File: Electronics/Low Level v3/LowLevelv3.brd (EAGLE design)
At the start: 117.3 x 68.1 mm, 53 parts, among them IC2 MCP4802, K1 ORWH-SH-105D1F,000, K3 ORWH-SH-105D1F,000, Q1 16MHz, T1 2N3904, T2 2N3904, U1 284512-4, U4 MCP2515, U5 MCP2551DIL08, X3 Motor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

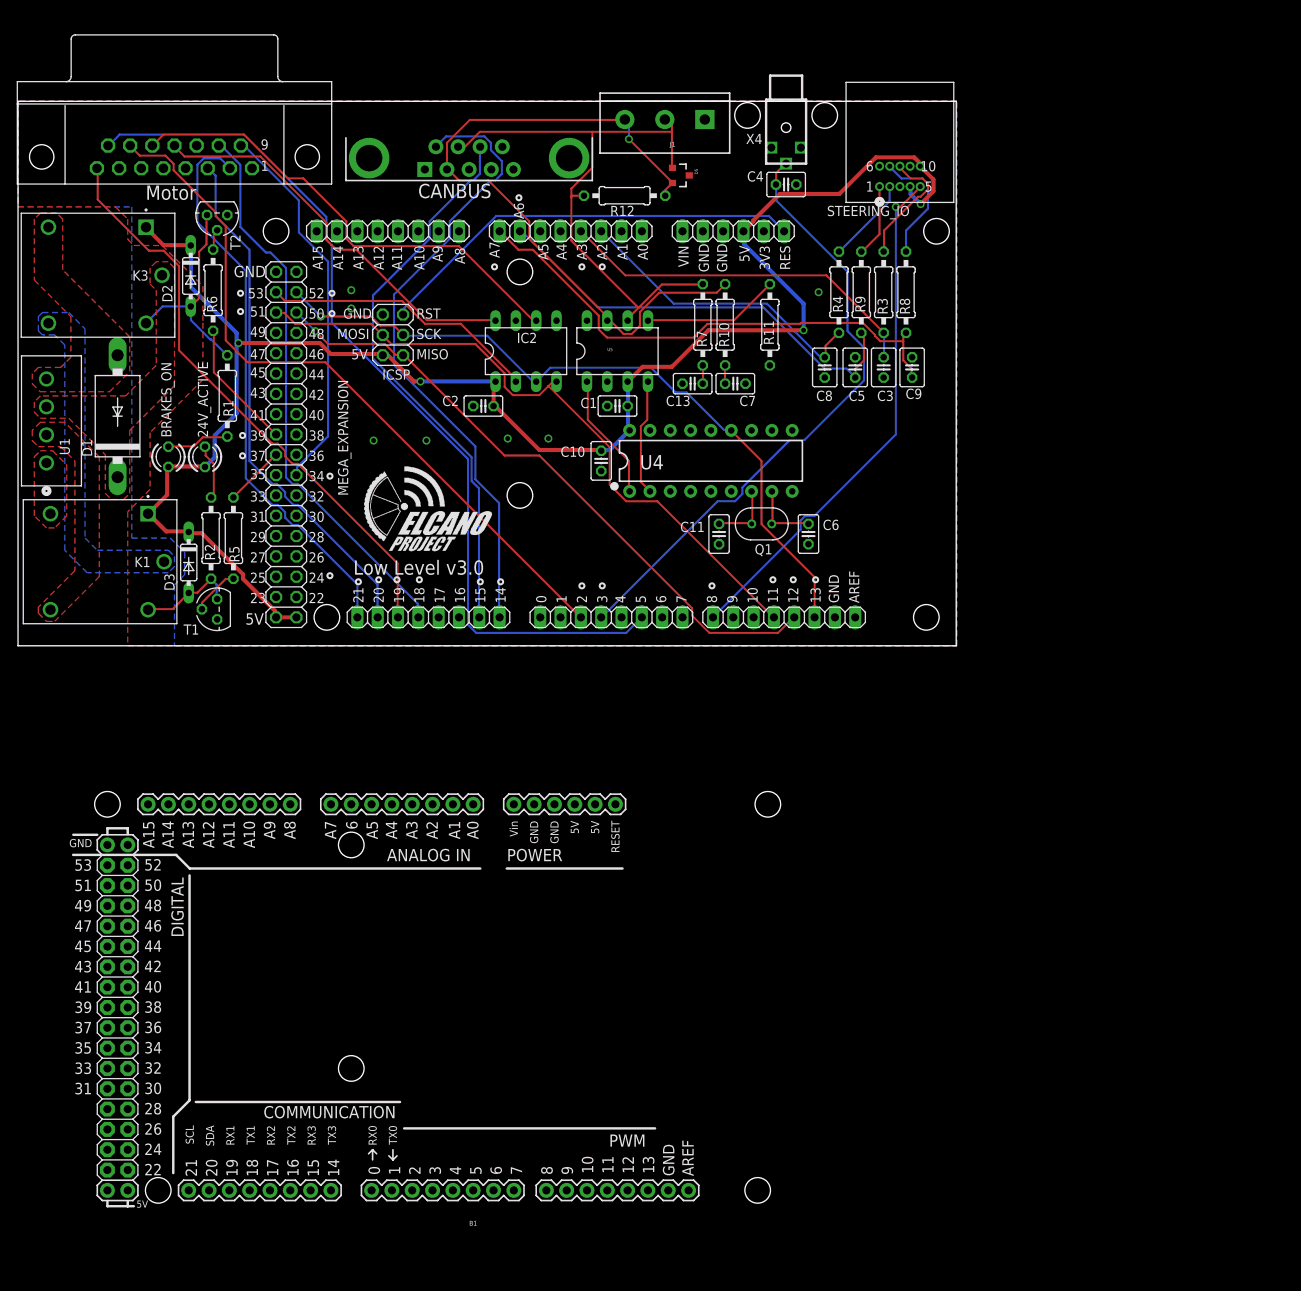
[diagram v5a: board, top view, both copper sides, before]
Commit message: Added reset button to top of board
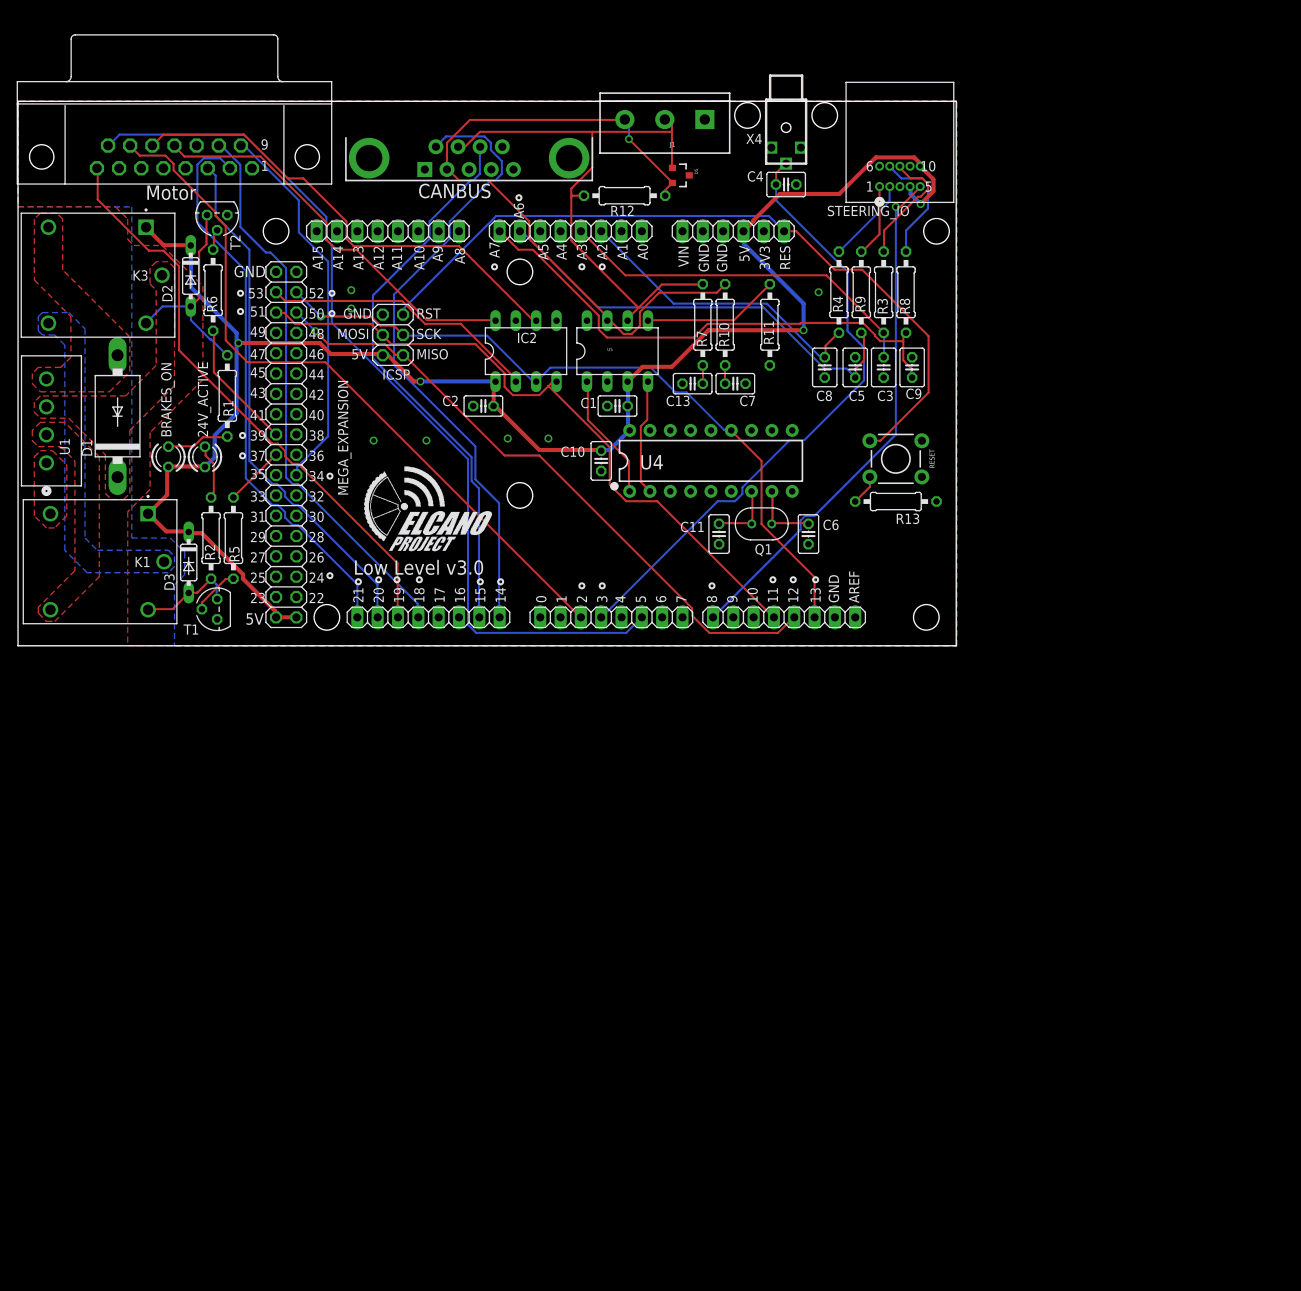
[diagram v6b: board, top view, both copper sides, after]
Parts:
- removed B1: ARDUINO_MEGA_R3FULL, SparkFun-Boards:ARDUINO_MEGA
- added R13: 1K, rcl:0207/10
- added RESET: MOMENTARY-SWITCH-SPST-PTH-6.0MM, SparkFun-Switches:TACTILE_SWITCH_PTH_6.0MM
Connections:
- new net N$1: R13.2, RESET.3
- net GND: now also R13.1
- net RESET: now also RESET.1
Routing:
- net RESET: track 53.9 -> 94.3 mm
- net N$1: track 0.00 -> 3.83 mm
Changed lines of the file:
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@@
 <attribute name="VALUE" x="77.3176" y="62.484" size="1.27" layer="27" ratio="10" rot="R180"/>
 </element>
-<element name="B1" library="SparkFun-Boards" library_urn="urn:adsk.eagle:library:509" package="ARDUINO_MEGA" package3d_urn="urn:adsk.eagle:package:37320/1" value="ARDUINO_MEGA_R3FULL" x="59.182" y="-38.354" smashed="yes" rot="R180">
-<attribute name="NAME" x="57.912" y="-66.294" size="0.6096" layer="25" font="vector" ratio="20" rot="R180" align="bottom-center"/>
-<attribute name="VALUE" x="59.182" y="-10.414" size="0.6096" layer="27" font="vector" ratio="20" rot="R180" align="top-center"/>
+<element name="RESET" library="SparkFun-Switches" library_urn="urn:adsk.eagle:library:535" package="TACTILE_SWITCH_PTH_6.0MM" package3d_urn="urn:adsk.eagle:package:40163/1" value="MOMENTARY-SWITCH-SPST-PTH-6.0MM" x="110.744" y="28.956" smashed="yes">
+<attribute name="NAME" x="115.57" y="28.956" size="0.6096" layer="25" font="vector" ratio="20" rot="R90" align="bottom-center"/>
+<attribute name="PROD_ID" value=" SWCH-08441" x="110.744" y="28.956" size="1.778" layer="27" display="off"/>
+<attribute name="SF_SKU" value="COM-00097" x="110.744" y="28.956" size="1.778" layer="27" display="off"/>
+</element>
+<element name="R13" library="rcl" library_urn="urn:adsk.eagle:library:334" package="0207/10" package3d_urn="urn:adsk.eagle:package:23491/2" value="1K" x="110.744" y="23.622" smashed="yes" rot="R180">
+<attribute name="NAME" x="113.792" y="22.098" size="1.27" layer="25" ratio="10" rot="R180"/>
+<attribute name="SPICEPREFIX" value="R" x="110.744" y="23.622" size="1.778" layer="27" rot="R180" display="off"/>
+<attribute name="VALUE" x="113.0046" y="24.257" size="1.27" layer="27" ratio="10" rot="R180"/>
 </element>
 </elements>
@@
 <via x="67.31" y="31.496" extent="1-16" drill="0.6096"/>
 <via x="101.092" y="49.784" extent="1-16" drill="0.6096"/>
+<contactref element="R13" pad="1"/>
 </signal>
 <signal name="RESET">
@@
 <wire x1="96.6978" y1="57.4929" x2="94.869" y2="59.3217" width="0.254" layer="16"/>
 <wire x1="96.6978" y1="57.4929" x2="96.774" y2="57.404" width="0.254" layer="16"/>
+<contactref element="RESET" pad="1"/>
+<wire x1="103.0986" y1="52.6034" x2="98.298" y2="57.404" width="0.254" layer="1"/>
+<wire x1="98.298" y1="57.404" x2="96.774" y2="57.404" width="0.254" layer="1"/>
+<wire x1="114.8334" y1="37.232475" x2="108.817525" y2="31.2166" width="0.254" layer="1"/>
+<wire x1="107.4928" y1="31.2166" x2="108.817525" y2="31.2166" width="0.254" layer="1"/>
+<wire x1="114.8334" y1="37.232475" x2="114.8334" y2="44.301525" width="0.254" layer="1"/>
+<wire x1="114.8334" y1="44.301525" x2="106.531525" y2="52.6034" width="0.254" layer="1"/>
+<wire x1="106.531525" y1="52.6034" x2="103.0986" y2="52.6034" width="0.254" layer="1"/>
 </signal>
 <signal name="SPEEDOMETER">
@@
 <wire x1="111.32904375" y1="60.452" x2="113.4745" y2="62.59745625" width="0.254" layer="1"/>
 </signal>
+<signal name="N$1">
+<contactref element="R13" pad="2"/>
+<contactref element="RESET" pad="3"/>
+<wire x1="105.664" y1="23.622" x2="107.4928" y2="25.4508" width="0.254" layer="1"/>
+<wire x1="107.4928" y1="25.4508" x2="107.4928" y2="26.6954" width="0.254" layer="1"/>
+</signal>
 </signals>

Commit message: Many LLBv3 updates in one!
re-arranged inerrupt pins to share a PCI ISR, added RC circuit to MCP2515 per datasheet, replaced impossible capacitor, re-arranged oscilator layout
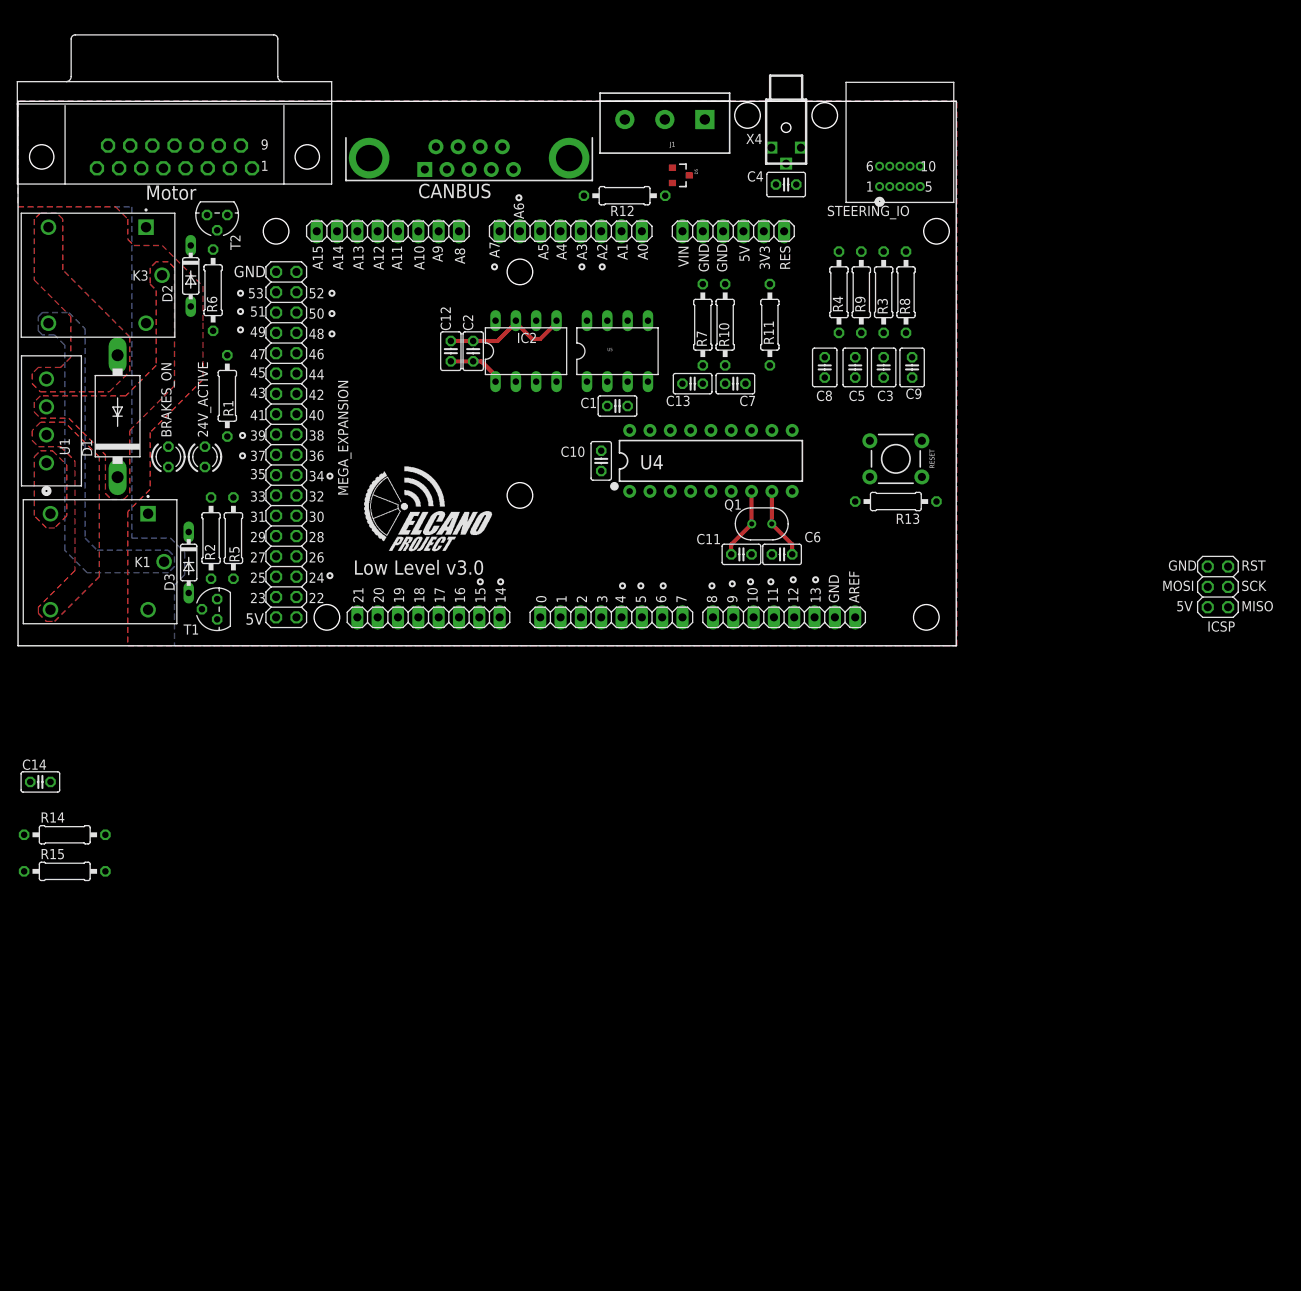
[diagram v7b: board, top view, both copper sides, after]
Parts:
- added C12, C14: 0.1uF, rcl:C025-025X050
- added R14: 1K, rcl:0207/10
- added R15: 20K, rcl:0207/10
- C11, C6: value 22pF -> 33pF
- C2: value 0.2uF -> 0.1uF
- moved ICSP 107.8 mm to (151.0, 13.0)
- moved C2 6.97 mm to (57.9, 42.4), turned to 90 degrees
- moved C6 4.17 mm to (96.5, 17.0), turned to 180 degrees
- moved C11 3.78 mm to (91.4, 17.0), turned to 0 degrees
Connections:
- net SL_RET renamed L_RET
- net SL_RTN renamed L_RTN_GND
- net SR_RET renamed R_RET
- net SR_RTN renamed R_RTN_GND
- removed net 3MISO: DIGITAL_8-13.5, ICSP.1, MEGA_EXPANSION.6
- removed net 3MOSI: DIGITAL_8-13.4, IC2.4, ICSP.4, MEGA_EXPANSION.5
- removed net CAN_CS: U4.16
- removed net SELECTAB: IC2.2, MEGA_EXPANSION.3
- new net CAN_SS: MEGA_EXPANSION.7, U4.16
- new net DAC_SS: IC2.2, MEGA_EXPANSION.8
- new net L_SENSE: C8.1, R4.1
- new net N$4: C14.1, R14.2, R15.2
- new net R_SENSE: C3.1, R3.1
- new net SPI_SLAVE: MEGA_EXPANSION.3
- net 5V: now also C12.1, R15.1
- net CAN_INT: now also DIGITAL_0-7.5
- net EBIKECONTRL: now also DIGITAL_8-13.3; no longer DIGITAL_14-21.4
- net GND: now also C12.2, C14.2, DIGITAL_8-13.7
- net HALLPHASEA: now also DIGITAL_8-13.6; no longer DIGITAL_14-21.1
- net HALLPHASEB: now also DIGITAL_8-13.5; no longer DIGITAL_14-21.2
- net HALLPHASEC: now also DIGITAL_8-13.4; no longer DIGITAL_14-21.3
- net MISO: now also ICSP.1, MEGA_EXPANSION.6
- net MOSI: now also IC2.4, ICSP.4, MEGA_EXPANSION.5
- net RS: now also R14.1
- net SCK: no longer DIGITAL_8-13.6
- net SPEEDOMETER: now also DIGITAL_8-13.1; no longer DIGITAL_0-7.3
- net STEER_SERVO_PWM: now also DIGITAL_0-7.7; no longer DIGITAL_8-13.1
- net STR_L: no longer C8.1, R4.1
- net STR_R: no longer C3.1, R3.1
- net WHEELROTATION: now also DIGITAL_8-13.2; no longer DIGITAL_0-7.4
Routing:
- net 5V: track 214.4 -> 7.09 mm, vias 4 -> 0
- net WATCHDOG: track 113.4 -> 0.00 mm
- net RESET: track 94.3 -> 0.00 mm
- net SCK: track 90.7 -> 0.00 mm, vias 1 -> 0
- net SPEEDOMETER: track 89.9 -> 0.00 mm
- net CANL: track 87.6 -> 0.00 mm, vias 1 -> 0
- net 3MOSI: track 84.0 -> 0.00 mm
- net 3MISO: track 80.2 -> 0.00 mm, vias 1 -> 0
- net TX3: track 79.1 -> 0.00 mm
- net WHEELROTATION: track 77.8 -> 0.00 mm
- net HALLPHASEC: track 73.7 -> 0.00 mm
- net CANH: track 73.6 -> 0.00 mm
- net HALLPHASEA: track 70.6 -> 0.00 mm
- net EBIKECONTRL: track 70.3 -> 0.00 mm
- net RX3: track 70.1 -> 0.00 mm
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
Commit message: LLBv3 updates
replaced all thru-hole res/cap with SMD parts, arranged part grids, re-routed the board
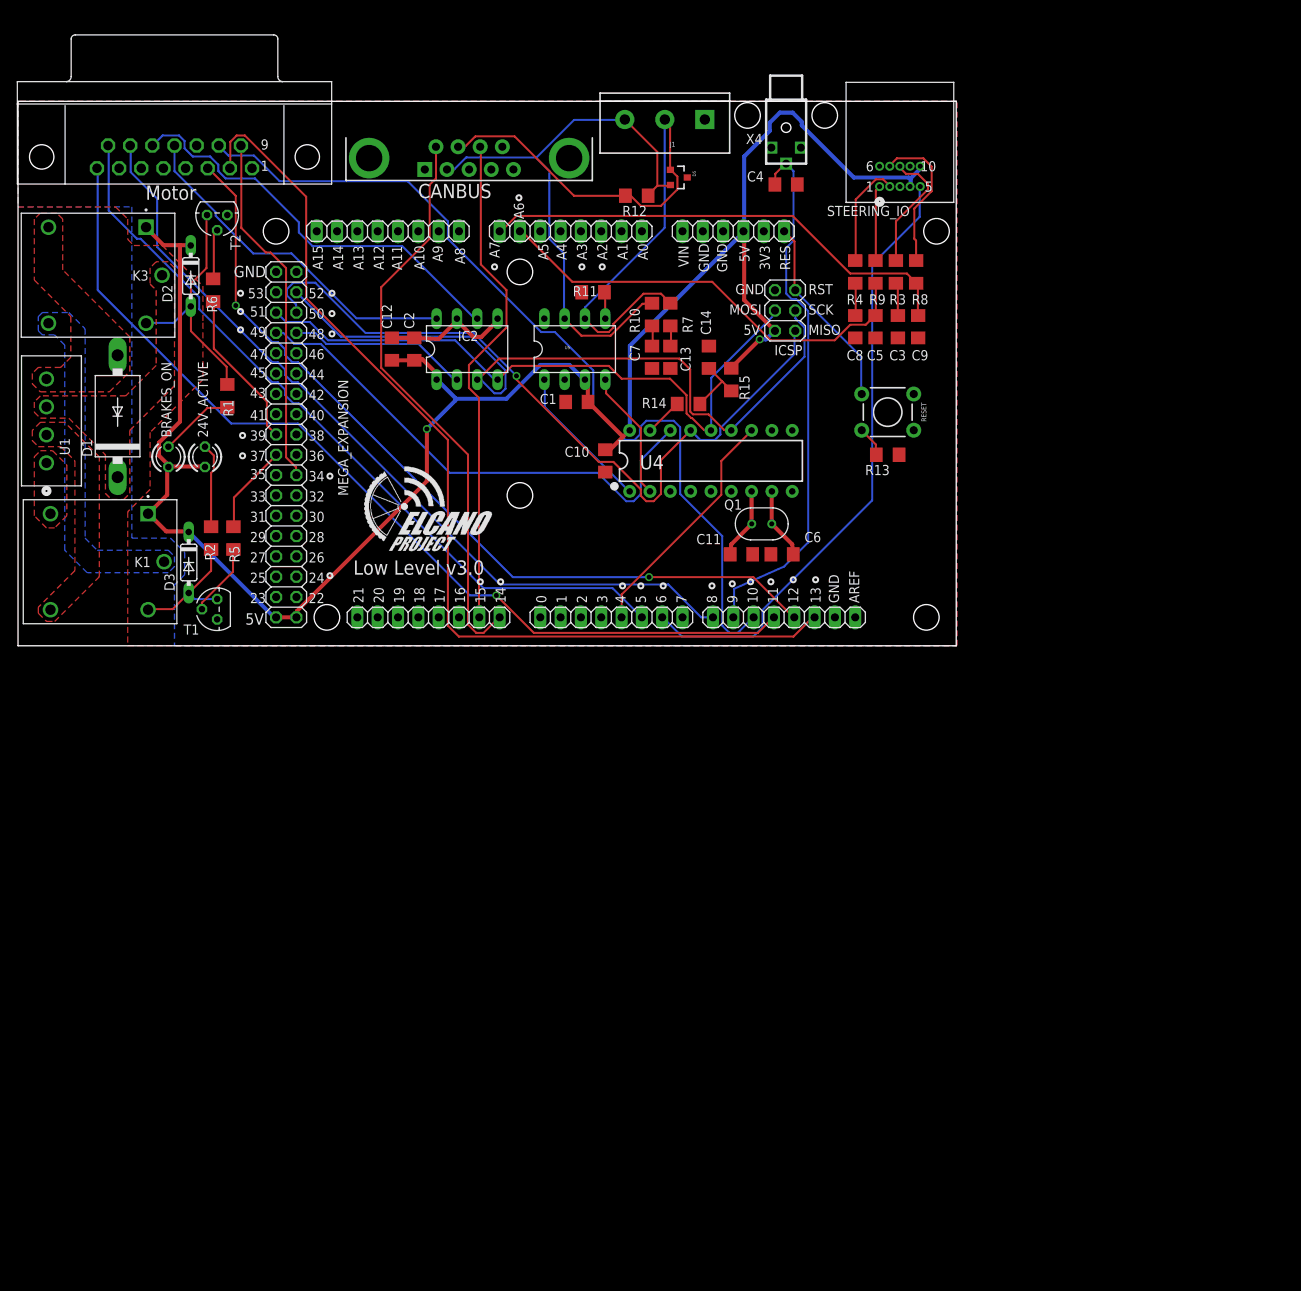
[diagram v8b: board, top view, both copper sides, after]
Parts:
- C1, C10, C11, C12, C13, C14, C2, C6, C7: device rcl:C025-025X050 -> resistor:C1206
- C3, C4, C5, C8, C9: device rcl:C025-030X050 -> resistor:C1206
- R1, R10, R11, R12, R13, R14, R15, R2, R3, R4, R5, R6, R7, R8, R9: device rcl:0207/10 -> resistor:R1206
- moved R15 103.5 mm to (90.2, 38.9), turned to 270 degrees
- moved C14 99.0 mm to (87.4, 41.7), turned to 90 degrees
- moved R14 94.8 mm to (84.8, 35.8)
- moved ICSP 64.2 mm to (96.9, 47.5)
- moved R11 22.5 mm to (72.9, 49.8), turned to 180 degrees
- moved C7 10.9 mm to (80.3, 41.7), turned to 270 degrees
- moved R10 9.23 mm to (80.3, 47.0)
- moved IC2 7.37 mm to (57.1, 42.7)
- moved C12 7.37 mm to (47.8, 42.7)
- moved C2 7.37 mm to (50.5, 42.7)
- moved C8 6.35 mm to (105.7, 45.5)
- moved RESET 5.93 mm to (109.7, 34.8)
- moved R13 5.93 mm to (109.7, 29.5)
- moved C5 5.68 mm to (108.2, 45.5), turned to 270 degrees
- moved C3 5.38 mm to (111.0, 45.5)
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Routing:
- net 5V: track 7.09 -> 241.2 mm, vias 0 -> 2
- net HALLPHASEA: track 0.00 -> 124.6 mm
- net HALLPHASEC: track 0.00 -> 118.4 mm, vias 0 -> 1
- net EBIKECONTRL: track 0.00 -> 110.9 mm
- net HALLPHASEB: track 0.00 -> 105.0 mm, vias 0 -> 2
- net SPEEDOMETER: track 0.00 -> 103.1 mm
- net WATCHDOG: track 0.00 -> 97.1 mm
- net SCK: track 0.00 -> 95.8 mm
- net MISO: track 0.00 -> 93.8 mm, vias 0 -> 1
- net CANH: track 0.00 -> 85.0 mm
- net MOSI: track 0.00 -> 81.5 mm
- net STEER_SERVO_PWM: track 0.00 -> 77.3 mm
- net CANL: track 0.00 -> 73.4 mm
- net TX3: track 0.00 -> 72.3 mm
- net WHEELROTATION: track 0.00 -> 67.6 mm
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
